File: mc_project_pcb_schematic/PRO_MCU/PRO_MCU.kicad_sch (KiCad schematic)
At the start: 14 parts, among them Q1 TN0702, Q2 TN0702, U1 Buttons_LED, U2 Chassis, U3 ItsyBitsy_NRF52840, U4 MPRLS, U5 waveshare_15867

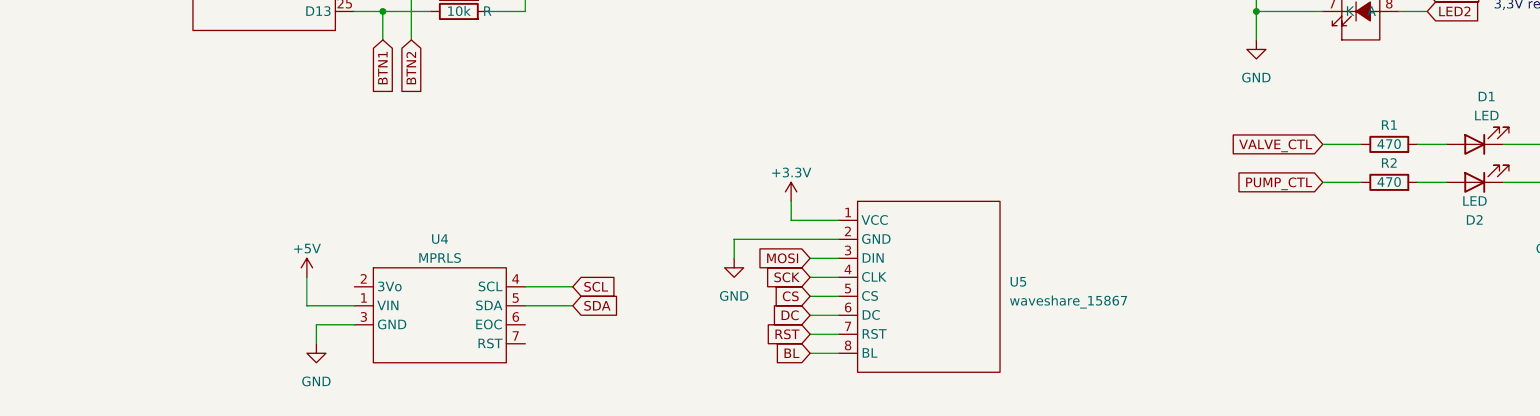
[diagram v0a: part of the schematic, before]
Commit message: new led resistor value and supply voltage filter
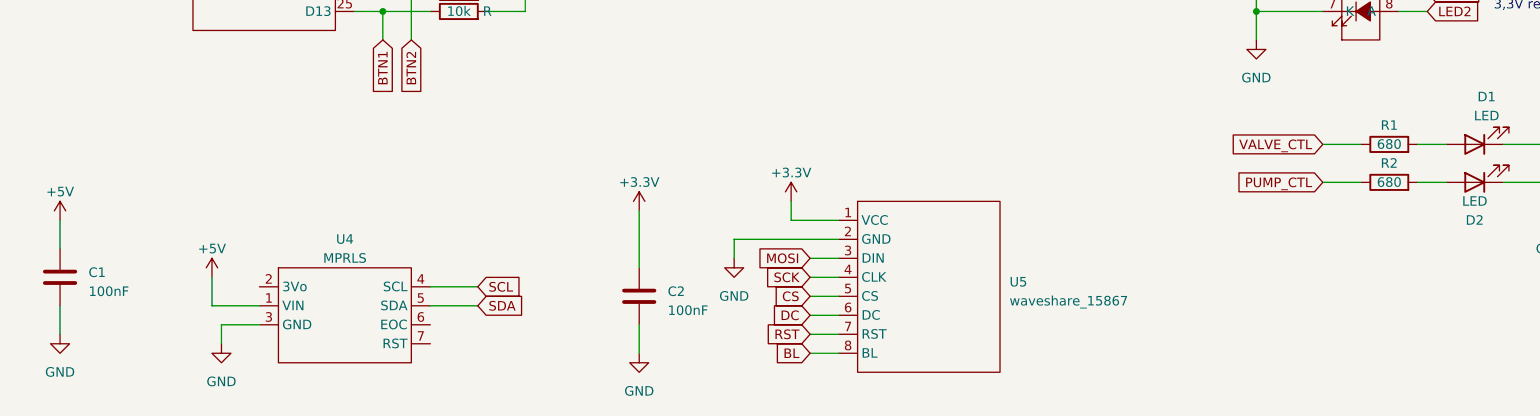
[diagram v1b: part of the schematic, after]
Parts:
- added C1, C2: 100nF, symbol Device:C
- R1, R2: value 470 -> 680
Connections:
- net +3.3V: now also C2.1
- net +5V: now also C1.1
- net GND: now also C1.2, C2.2
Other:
- moved on the sheet: U4

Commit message: new pinout
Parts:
- removed JP1: SolderJumper_3_Open, symbol Jumper:SolderJumper_3_Open
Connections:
- net +3.3V: now also U4.2 (3Vo)
- net +5V: no longer U4.1 (VIN)
- net BL: now also U3.5 (A0); no longer U3.7 (A2)
- net BTN1: now also U3.20 (D7); no longer U3.25 (D13)
- net CS: now also U3.8 (A3); no longer U3.21 (D9)
- net DC: now also U3.7 (A2); no longer U3.20 (D7)
- net LED1: now also U3.19 (D5_5V); no longer U3.5 (A0)
- net LED2: now also U3.23 (D11); no longer U3.6 (A1)
- net PUMP_CTL: now also U3.21 (D9)
- net RST: now also U3.6 (A1); no longer U3.8 (A3)
- net EOC: now reaches U4.6 (EOC)
- net EOC: now also U3.9 (A4)
- net MPRLS_RST: now reaches U4.7 (RST)
- net MPRLS_RST: now also U3.10 (A5)
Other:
- moved on the sheet: 10k
